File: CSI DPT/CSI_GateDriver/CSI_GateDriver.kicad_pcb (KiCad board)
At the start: 4 copper layers, 100 x 80 mm, 75 parts, among them J1 SSW-102-01-G-D, J2 Conn_02x08_Odd_Even, J3 SSW-102-01-G-D, Q3 DMP3099L, U1 UCC23513QDWYRQ1, U10 UCC23513QDWYRQ1, U11 MGJ2D121802SC, U12 LDK130-12_SOT23_SOT353, U2 MGJ2D121802SC, U3 MGJ2D121802SC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

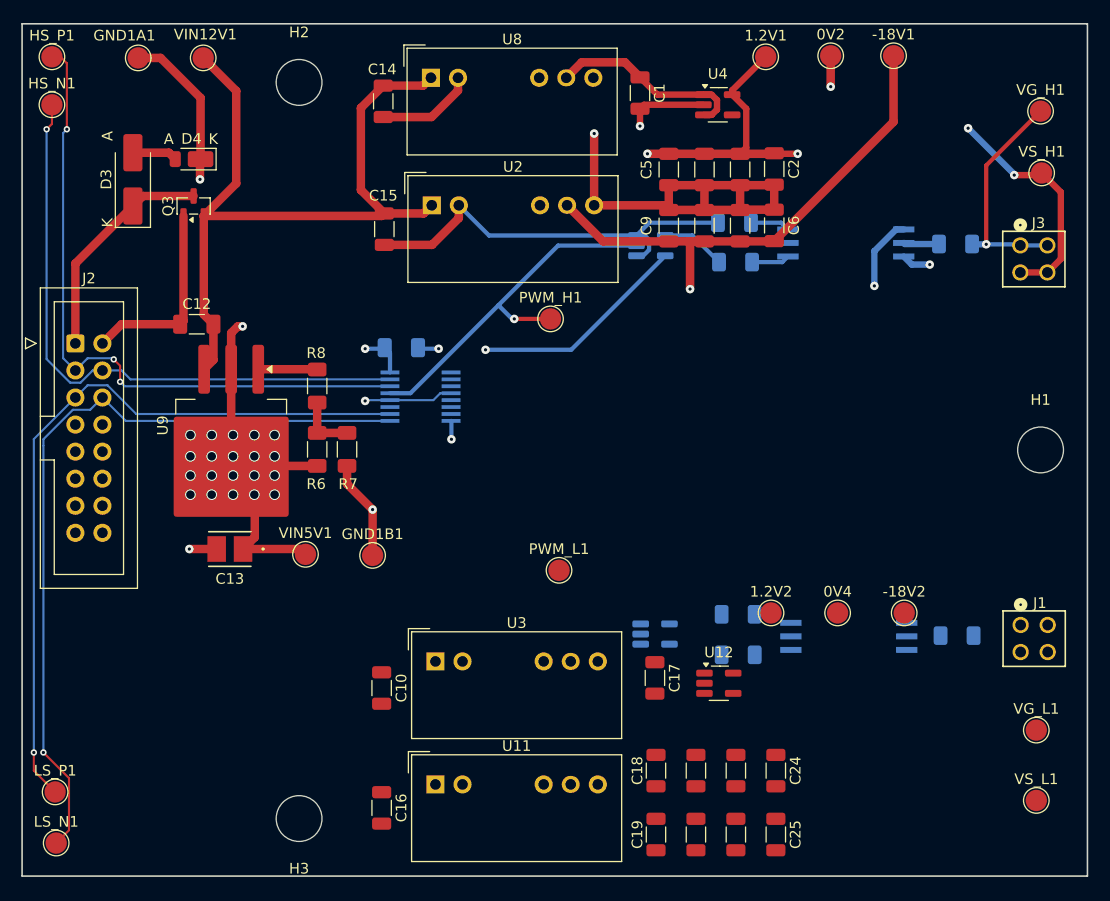
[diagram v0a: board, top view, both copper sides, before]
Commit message: Completed gate driver V1
1. finished the PCB layout of gate driver V1, waiting for feedback
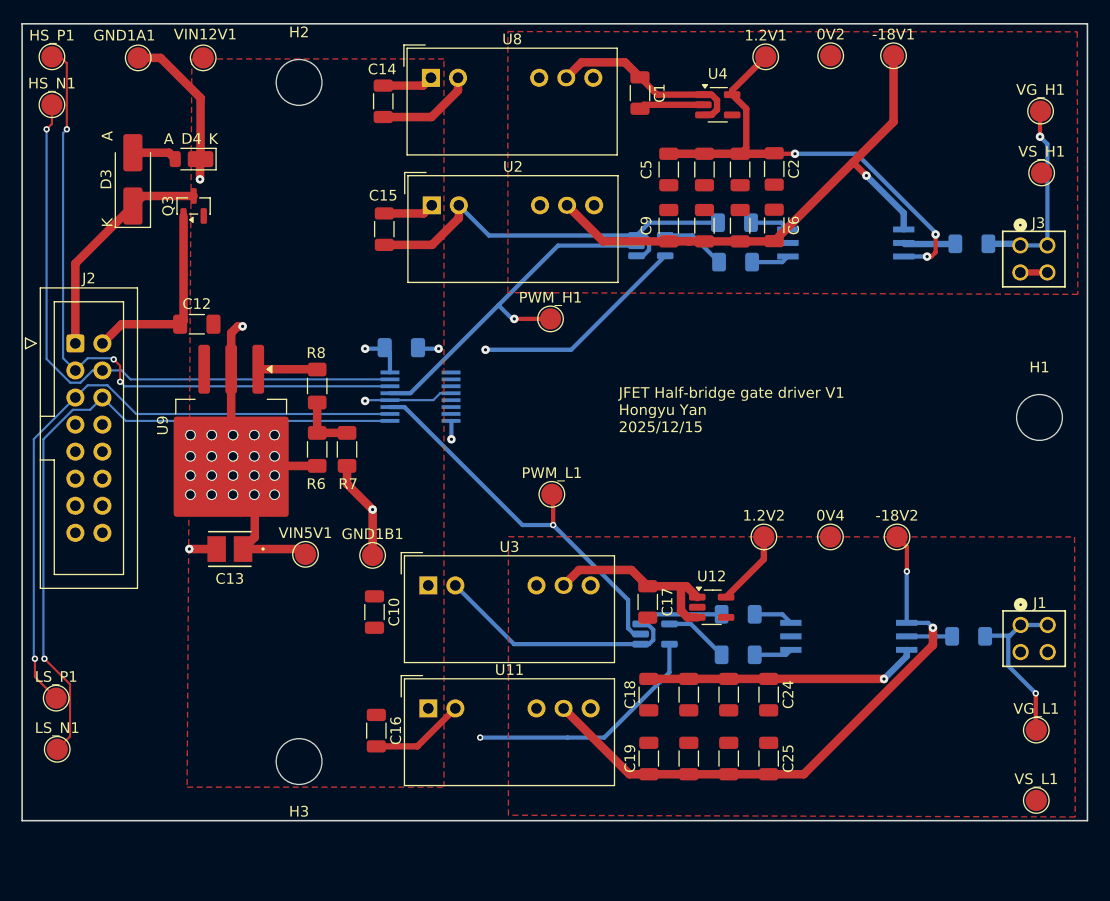
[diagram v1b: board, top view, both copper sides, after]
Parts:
- moved LS_N1 8.80 mm to (69.3, 130.0)
- moved LS_P1 8.80 mm to (69.2, 125.2)
- moved C16 7.27 mm to (99.2, 128.2)
- moved -18V2 7.16 mm to (148.1, 110.1)
- moved 0V4 7.16 mm to (141.9, 110.1)
- moved 1.2V2 7.16 mm to (135.6, 110.1)
- moved PWM_L1 7.16 mm to (115.7, 106.1)
- moved C20 7.16 mm to (128.6, 124.9)
- moved C21 7.16 mm to (128.6, 130.9)
- moved C22 7.16 mm to (132.3, 124.9)
- moved C23 7.16 mm to (132.3, 130.9)
- moved C24 7.16 mm to (136.1, 124.9)
- moved C25 7.16 mm to (136.1, 130.9)
- moved U12 7.16 mm to (130.7, 116.7)
- moved C10 7.16 mm to (99.1, 117.1)
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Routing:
- net /Gate_Driver/0V_H: track 75.7 -> 8.65 mm, vias 5 -> 0
- net /Gate_Driver/VIN12V: track 72.9 -> 9.55 mm
- net /Gate_Driver/-18V_L: track 0.00 -> 55.0 mm, vias 0 -> 2
- net GND1: track 106.3 -> 146.6 mm
- net /Gate_Driver/PWM_L: track 0.00 -> 36.8 mm, vias 0 -> 1
- net /Gate_Driver/1.2V_L: track 0.00 -> 32.8 mm, vias 0 -> 1
- net /Gate_Driver/VIN5V: track 61.4 -> 84.4 mm, vias 24 -> 25
- net Net-(U12-EN): track 0.00 -> 18.3 mm
- net /Gate_Driver/VGATE_L: track 0.00 -> 16.3 mm, vias 0 -> 1
- net /Gate_Driver/1.2V_H: track 28.1 -> 44.4 mm
- net /Gate_Driver/LS_N: track 74.5 -> 65.7 mm
- net /Gate_Driver/LS_P: track 70.6 -> 61.8 mm
- net Net-(U6-Y): track 0.00 -> 6.10 mm
- net Net-(U10-VOUT): track 0.00 -> 4.26 mm
- net Net-(U10-CATHODE): track 0.00 -> 3.73 mm
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- added copper zone on F.Cu, net /Gate_Driver/0V_H
- added copper zone on F.Cu, net /Gate_Driver/0V_L
- added copper zone on F.Cu, net /Gate_Driver/VIN12V
- removed copper zone on In1.Cu, net /Gate_Driver/-18V_H
- removed copper zone on In1.Cu, net /Gate_Driver/0V_H
- removed copper zone on In1.Cu, net /Gate_Driver/1.2V_H
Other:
- board size 100 x 80 mm -> 100 x 74.8 mm
- board text added: "JFET Half-bridge gate driver V1 Hongyu Yan 2025/12/15"

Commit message: CSI Tester V1 Completed
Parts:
- moved J1 0.30 mm to (161.0, 119.9)
- moved J3 0.08 mm to (161.0, 83.9)
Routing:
- net /Gate_Driver/VGATE_L: track 16.3 -> 17.4 mm
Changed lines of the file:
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@@
 	(footprint "Gate_Driver:CON4_2X2_TU_SSQ"
 		(layer "F.Cu")
-		(at 160.97 83.97 180)
+		(at 161 83.9 180)
 		(tags "SSW-102-01-G-D ")
 		(property "Reference" "J3"
@@
 	(footprint "Gate_Driver:CON4_2X2_TU_SSQ"
 		(layer "F.Cu")
-		(at 161 119.6 180)
+		(at 161 119.9 180)
 		(tags "SSW-102-01-G-D ")
 		(property "Reference" "J1"
@@
 	(segment
 		(start 156.7 82.55)
-		(end 159.55 82.55)
+		(end 159.65 82.55)
 		(width 0.6)
 		(layer "B.Cu")
@@
 	)
 	(segment
-		(start 162.24 73.19)
-		(end 161.55 72.5)
-		(width 0.4)
-		(layer "B.Cu")
-		(net 9)
-	)
-	(segment
-		(start 159.55 82.55)
-		(end 159.7 82.7)
+		(start 162.27 82.63)
+		(end 162.27 73.22)
 		(width 0.6)
 		(layer "B.Cu")
@@
 	)
 	(segment
-		(start 159.7 82.7)
-		(end 162.24 82.7)
-		(width 0.4)
+		(start 159.65 82.55)
+		(end 159.73 82.63)
+		(width 0.6)
 		(layer "B.Cu")
 		(net 9)
 	)
 	(segment
-		(start 162.24 82.7)
-		(end 162.24 73.19)
-		(width 0.4)
+		(start 162.27 73.22)
+		(end 161.55 72.5)
+		(width 0.6)
 		(layer "B.Cu")
 		(net 9)
 	)
 	(segment
-		(start 159.6 82.6)
-		(end 159.7 82.7)
-		(width 0.4)
+		(start 159.73 82.63)
+		(end 162.27 82.63)
+		(width 0.6)
 		(layer "B.Cu")
 		(net 9)
@@
 	)
 	(segment
-		(start 158.567 119.493)
-		(end 158.567 122.167)
-		(width 0.4)
-		(layer "B.Cu")
-		(net 44)
-	)
-	(segment
-		(start 158.73 119.33)
-		(end 158.567 119.493)
-		(width 0.4)
+		(start 159.73 118.63)
+		(end 158.467 119.893)
+		(width 0.6)
 		(layer "B.Cu")
 		(net 44)
 	)
 	(segment
-		(start 158.73 119.33)
-		(end 159.73 118.33)
-		(width 0.4)
+		(start 159.73 118.63)
+		(end 162.27 118.63)
+		(width 0.6)
 		(layer "B.Cu")
 		(net 44)
 	)
 	(segment
-		(start 159.73 118.33)
-		(end 162.27 118.33)
-		(width 0.4)
+		(start 156.4 119.4)
+		(end 158.96 119.4)
+		(width 0.6)
 		(layer "B.Cu")
 		(net 44)
 	)
 	(segment
-		(start 156.4 119.4)
-		(end 156.47 119.33)
-		(width 0.4)
+		(start 158.467 119.893)
+		(end 158.467 122.067)
+		(width 0.6)
 		(layer "B.Cu")
 		(net 44)
 	)
 	(segment
-		(start 156.47 119.33)
-		(end 158.73 119.33)
-		(width 0.4)
+		(start 158.96 119.4)
+		(end 159.73 118.63)
+		(width 0.6)
 		(layer "B.Cu")
 		(net 44)
 	)
 	(segment
-		(start 158.567 122.167)
+		(start 158.467 122.067)
 		(end 161.15 124.75)
-		(width 0.4)
+		(width 0.6)
 		(layer "B.Cu")
 		(net 44)

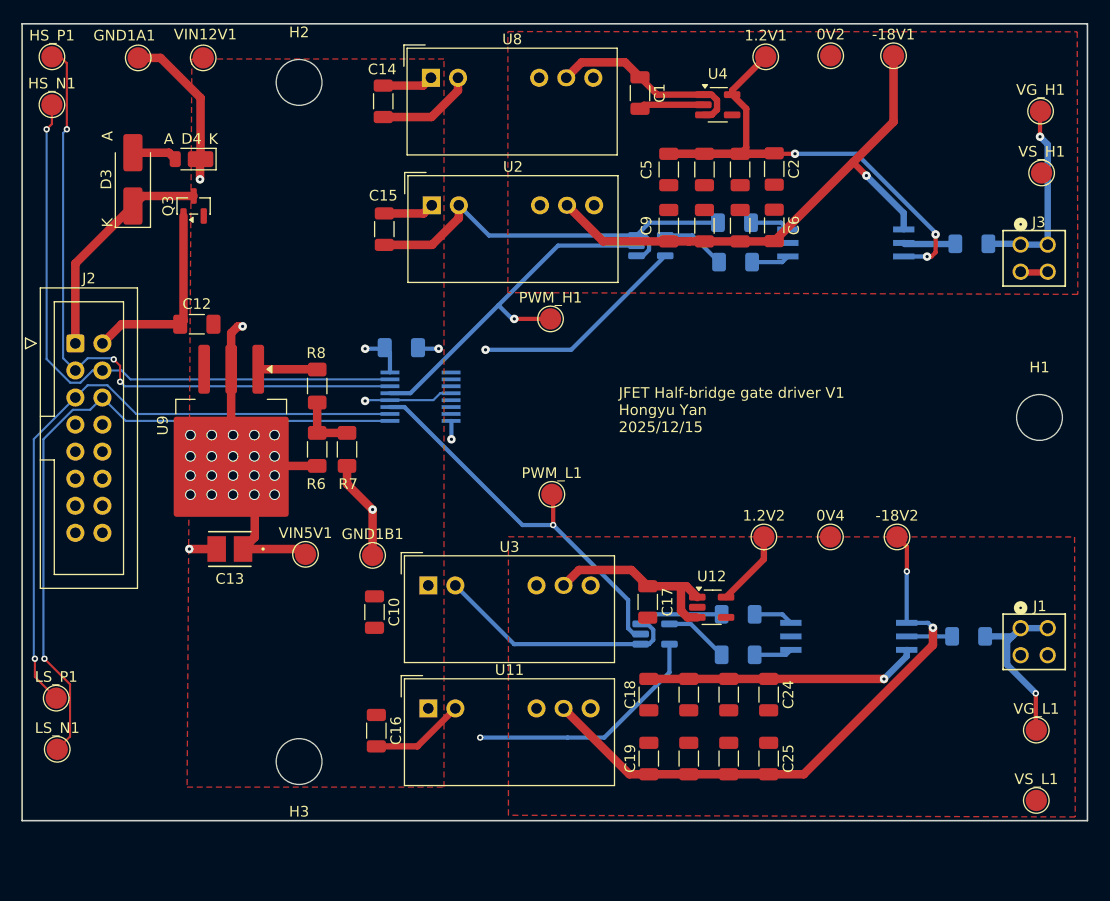
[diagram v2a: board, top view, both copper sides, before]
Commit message: Size down the boards
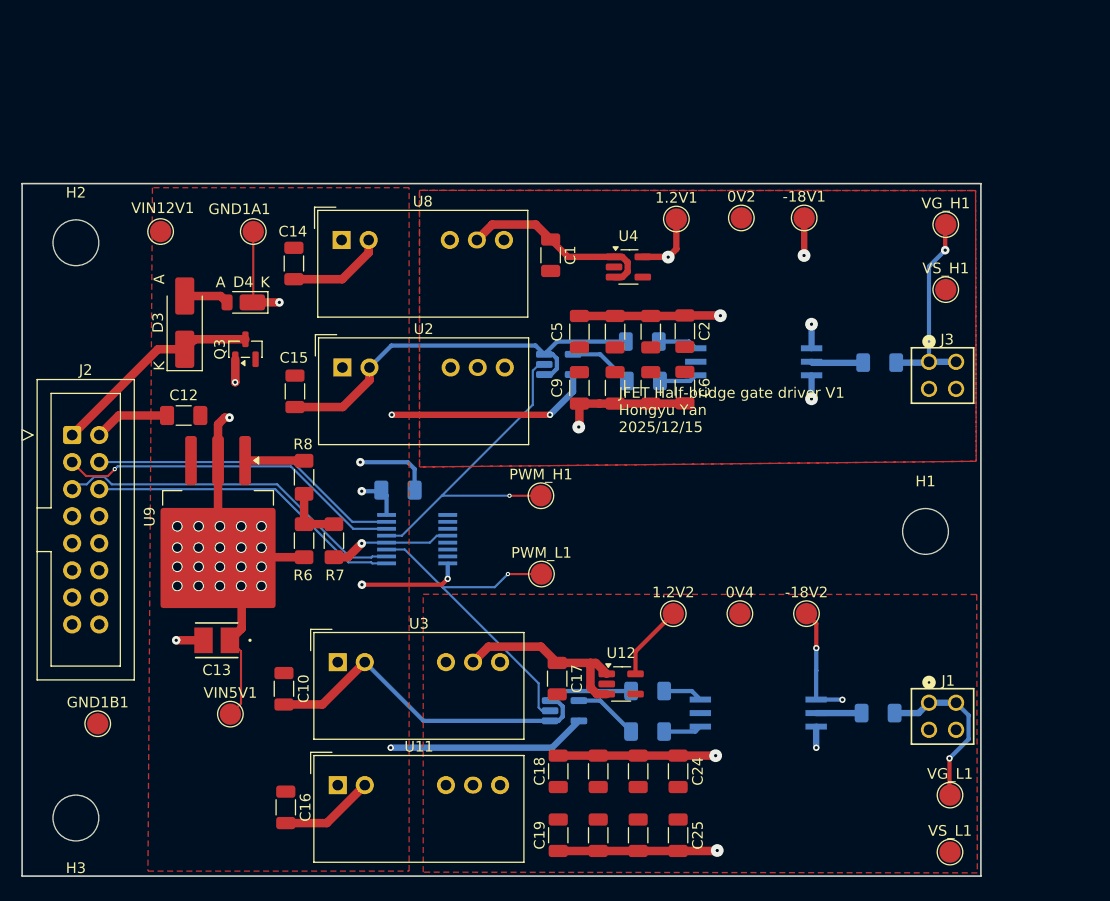
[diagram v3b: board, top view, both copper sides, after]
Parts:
- removed HS_N1: HS_N, TestPoint:TestPoint_Pad_D2.0mm
- removed HS_P1: HS_P, TestPoint:TestPoint_Pad_D2.0mm
- removed LS_N1: LS_N, TestPoint:TestPoint_Pad_D2.0mm
- removed LS_P1: LS_P, TestPoint:TestPoint_Pad_D2.0mm
- moved GND1B1 30.3 mm to (73.1, 127.6)
- moved H2 25.8 mm to (71.0, 82.5)
- moved H3 21.6 mm to (71.0, 136.4)
- moved GND1A1 19.6 mm to (87.7, 81.4)
- moved C8 17.4 mm to (121.7, 96.1)
- moved C14 17.4 mm to (91.5, 84.4)
- moved C15 17.4 mm to (91.6, 96.4)
- moved C7 17.4 mm to (125.0, 96.1)
- moved C9 17.4 mm to (118.3, 96.1)
- moved -18V1 17.4 mm to (139.4, 80.1)
- moved 0V2 17.4 mm to (133.5, 80.1)
- moved 1.2V1 17.4 mm to (127.4, 80.2)
- moved C4 17.4 mm to (121.7, 90.8)
- moved U4 17.4 mm to (122.9, 84.7)
- moved C1 17.4 mm to (115.6, 83.6)
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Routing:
- net /Gate_Driver/LS_N: track 65.7 -> 29.9 mm, vias 1 -> 0
- net /Gate_Driver/-18V_H: track 51.2 -> 17.9 mm, vias 1 -> 3
- net /Gate_Driver/HS_P: track 63.1 -> 32.9 mm, vias 3 -> 1
- net /Gate_Driver/-18V_L: track 55.0 -> 25.9 mm, vias 2 -> 3
- net /Gate_Driver/HS_N: track 58.0 -> 29.3 mm, vias 1 -> 0
- net /Gate_Driver/LS_P: track 61.8 -> 33.2 mm, vias 1 -> 0
- net /Gate_Driver/1.2V_H: track 44.4 -> 21.8 mm
- net GND1: track 146.6 -> 134.9 mm
- net /Gate_Driver/VIN5V: track 84.4 -> 94.2 mm, vias 25 -> 27
- net /Gate_Driver/VIN12V: track 9.55 -> 0.00 mm
- net /Gate_Driver/1.2V_L: track 32.8 -> 23.9 mm, vias 1 -> 2
- net /Gate_Driver/0V_H: track 8.65 -> 0.00 mm
- net /Gate_Driver/PWM_L: track 36.8 -> 32.8 mm
- net /Gate_Driver/PWM_H: track 34.3 -> 32.6 mm
- net /Gate_Driver/VGATE_L: track 17.4 -> 16.1 mm
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- added copper zone on F.Cu, net /Gate_Driver/-18V_H
- added copper zone on In1.Cu, net /Gate_Driver/-18V_H
- added copper zone on In1.Cu, net /Gate_Driver/-18V_L
- added copper zone on In2.Cu, net /Gate_Driver/1.2V_H
- added copper zone on In2.Cu, net /Gate_Driver/1.2V_L
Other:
- board size 100 x 74.8 mm -> 90 x 65 mm
